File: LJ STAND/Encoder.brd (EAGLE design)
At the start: 24 x 17.4 mm, 4 parts, among them IC1 A1301LH, IC2 A1301LH

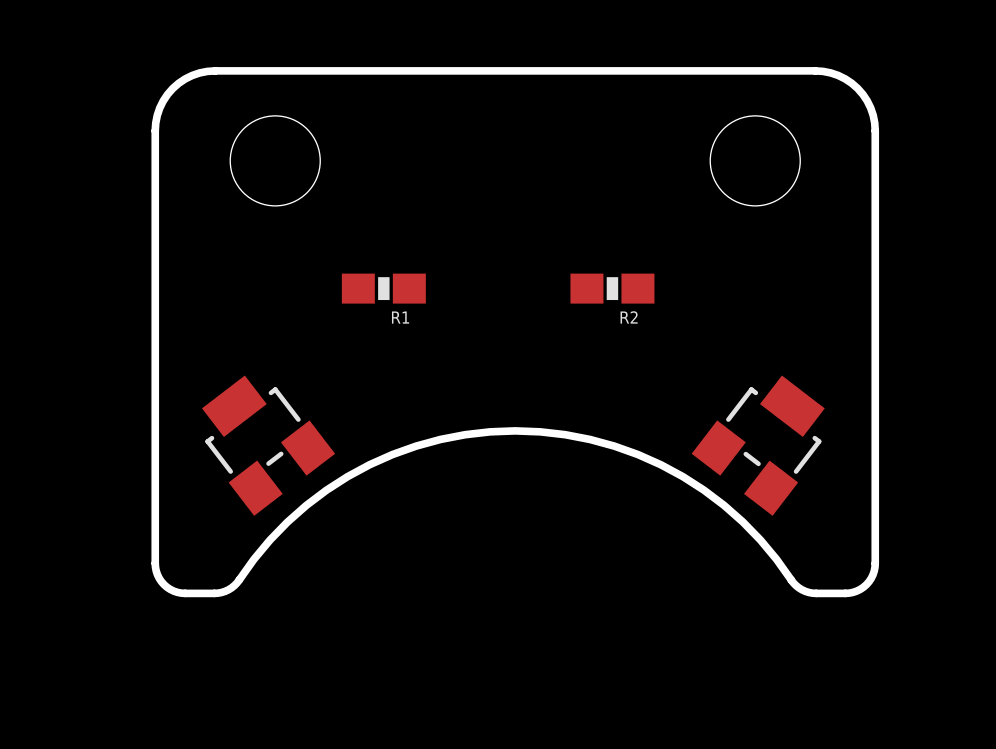
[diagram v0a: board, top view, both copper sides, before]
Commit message: Main & light schematics, preliminary board layout
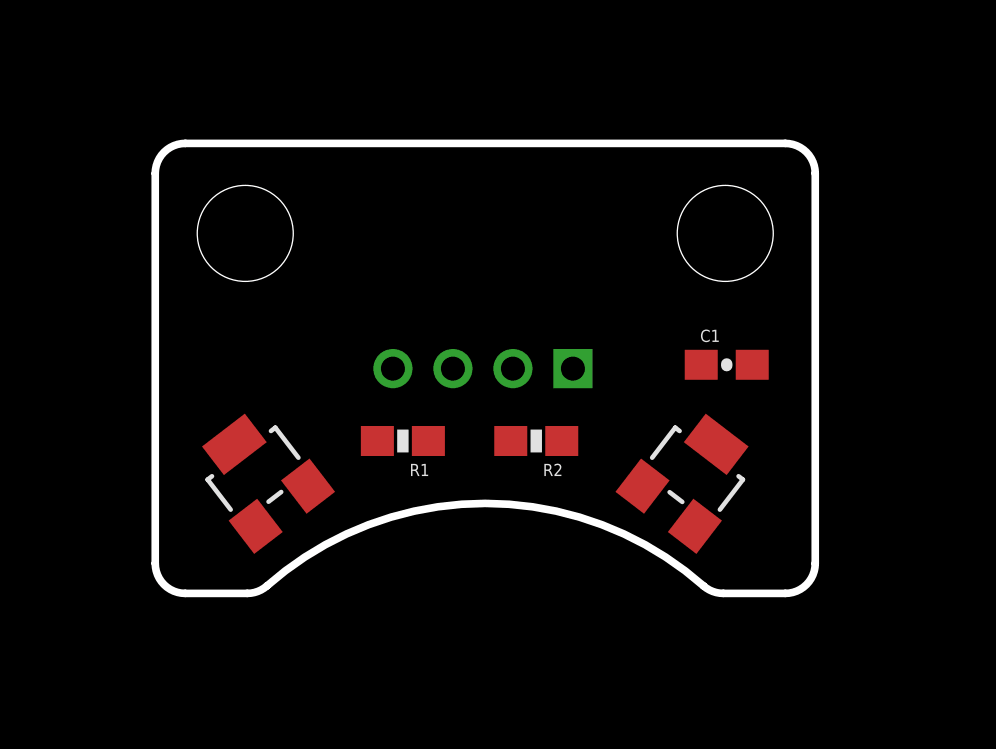
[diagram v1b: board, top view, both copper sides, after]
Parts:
- added C1: 0.1uF, SparkFun-Capacitors:0603-CAP
- added J1: (no value), jst-ph:B4B-PH-K-S
- moved R2 5.68 mm to (12.7, 5.08)
- moved R1 5.12 mm to (8.26, 5.08)
- moved IC2 2.84 mm to (17.9, 3.94)
- moved IC1 1.27 mm to (3.43, 3.94)
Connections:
- net GND: now also C1.2, J1.1
- net OUTA: now also J1.3
- net OUTB: now also J1.2
- net VCC: now also C1.1, J1.4
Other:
- board size 24 x 17.4 mm -> 22 x 15 mm
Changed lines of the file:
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@@
 <?xml version="1.0" encoding="utf-8"?>
 <!DOCTYPE eagle SYSTEM "eagle.dtd">
-<eagle version="8.5.0">
+<eagle version="8.6.3">
 <drawing>
 <settings>
@@
 <setting verticaltext="up"/>
 </settings>
-<grid distance="50" unitdist="mil" unit="mil" style="lines" multiple="1" display="no" altdistance="5" altunitdist="mil" altunit="mil"/>
+<grid distance="25" unitdist="mil" unit="mil" style="lines" multiple="1" display="no" altdistance="5" altunitdist="mil" altunit="mil"/>
 <layers>
 <layer number="1" name="Top" color="4" fill="1" visible="yes" active="yes"/>
@@
 <layer number="112" name="tSilk" color="7" fill="1" visible="yes" active="yes"/>
 <layer number="113" name="IDFDebug" color="4" fill="1" visible="yes" active="yes"/>
+<layer number="114" name="Badge_Outline" color="7" fill="1" visible="yes" active="yes"/>
+<layer number="115" name="ReferenceISLANDS" color="7" fill="1" visible="yes" active="yes"/>
 <layer number="116" name="Patch_BOT" color="9" fill="4" visible="yes" active="yes"/>
+<layer number="118" name="Rect_Pads" color="7" fill="1" visible="yes" active="yes"/>
 <layer number="121" name="_tsilk" color="7" fill="1" visible="yes" active="yes"/>
 <layer number="122" name="_bsilk" color="7" fill="1" visible="yes" active="yes"/>
@@
 </layers>
 <board>
-<fusionsync huburn="a.cGVyc29uYWw6dWUyYWQzYjQx" projecturn="a.cGVyc29uYWw6dWUyYWQzYjQxIzIwMTcxMTAzMTAyMTc0NDI2" f3durn="urn:adsk.wipprod:dm.lineage:2KaG5NQ2SkW999M1W_C92Q" pcbguid="16a91ec9-6d86-41c8-a764-7d3732d7a789" lastpulledtime="2018-02-09T08:51:01Z" lastsyncedchangeguid="f0354a51-48ac-62f3-02b0-e84390e50f97"/>
+<fusionsync huburn="a.cGVyc29uYWw6dWUyYTBjMzI3" projecturn="a.cGVyc29uYWw6dWUyYTBjMzI3IzIwMTgwMjIxMTE4OTc1ODMx" f3durn="urn:adsk.wipprod:dm.lineage:Les9lctRTmKd2iDqQ8lVyw" pcbguid="9d74a9eb-0c4b-4d1f-9566-72efe2af230e" lastpulledtime="2018-02-23T02:58:26Z" lastsyncedchangeguid="d0473fdc-9464-a69d-910f-55a8cdc6a555"/>
 <plain>
-<hole x="4" y="14.41699375" drill="3"/>
-<hole x="20" y="14.41699375" drill="3"/>
-<wire x1="21.1971" y1="0.4514" x2="22.0331" y2="0" width="0.254" layer="20" curve="56.730093"/>
-<wire x1="22.0331" y1="0" x2="23" y2="0" width="0.254" layer="20"/>
-<wire x1="23" y1="0" x2="24" y2="1" width="0.254" layer="20" curve="90"/>
-<wire x1="24" y1="1" x2="24" y2="15.417" width="0.254" layer="20"/>
-<wire x1="24" y1="15.417" x2="22" y2="17.417" width="0.254" layer="20" curve="90"/>
-<wire x1="22" y1="17.417" x2="2" y2="17.417" width="0.254" layer="20"/>
-<wire x1="2" y1="17.417" x2="0" y2="15.417" width="0.254" layer="20" curve="90"/>
-<wire x1="0" y1="15.417" x2="0" y2="1" width="0.254" layer="20"/>
+<hole x="3" y="12" drill="3.2"/>
+<hole x="19" y="12" drill="3.2"/>
+<wire x1="22" y1="1" x2="22" y2="14" width="0.254" layer="20"/>
+<wire x1="22" y1="14" x2="21" y2="15" width="0.254" layer="20" curve="90"/>
+<wire x1="21" y1="15" x2="1" y2="15" width="0.254" layer="20"/>
+<wire x1="1" y1="15" x2="0" y2="14" width="0.254" layer="20" curve="90"/>
+<wire x1="0" y1="14" x2="0" y2="1" width="0.254" layer="20"/>
 <wire x1="0" y1="1" x2="1" y2="0" width="0.254" layer="20" curve="90"/>
-<wire x1="1" y1="0" x2="1.9669" y2="0" width="0.254" layer="20"/>
-<wire x1="1.9669" y1="0" x2="2.8029" y2="0.4514" width="0.254" layer="20" curve="56.730093"/>
-<wire x1="2.8029" y1="0.4514" x2="21.1971" y2="0.4514" width="0.254" layer="20" curve="-113.460187"/>
+<wire x1="1" y1="0" x2="3.063" y2="0" width="0.254" layer="20"/>
+<wire x1="3.063" y1="0" x2="3.724" y2="0.25" width="0.254" layer="20" curve="41.41"/>
+<wire x1="3.724" y1="0.25" x2="18.276" y2="0.25" width="0.254" layer="20" curve="-82.819"/>
+<wire x1="18.276" y1="0.25" x2="18.937" y2="0" width="0.254" layer="20" curve="41.41"/>
+<wire x1="18.937" y1="0" x2="21" y2="0" width="0.254" layer="20"/>
+<wire x1="21" y1="0" x2="22" y2="1" width="0.254" layer="20" curve="90"/>
 </plain>
 <attributes>
@@
 </autorouter>
 <elements>
-<element name="IC1" library="allegro" library_urn="urn:adsk.eagle:library:93" package="SOT23-W" package3d_urn="urn:adsk.eagle:package:3443/1" value="A1301LH" x="3.429" y="5.207" smashed="yes" rot="R37.5">
-<attribute name="MF" value="ALLEGRO MICROSYSTEMS, INC." x="3.429" y="5.207" size="1.778" layer="27" rot="R37.5" display="off"/>
-<attribute name="MPN" value="A1301ELHLT-T" x="3.429" y="5.207" size="1.778" layer="27" rot="R37.5" display="off"/>
-<attribute name="OC_FARNELL" value="1198084" x="3.429" y="5.207" size="1.778" layer="27" rot="R37.5" display="off"/>
-<attribute name="OC_NEWARK" value="31K6634" x="3.429" y="5.207" size="1.778" layer="27" rot="R37.5" display="off"/>
+<element name="IC1" library="allegro" library_urn="urn:adsk.eagle:library:93" package="SOT23-W" package3d_urn="urn:adsk.eagle:package:3443/1" value="A1301LH" x="3.429" y="3.937" smashed="yes" rot="R37.5">
+<attribute name="MF" value="ALLEGRO MICROSYSTEMS, INC." x="3.429" y="3.937" size="1.778" layer="27" rot="R37.5" display="off"/>
+<attribute name="MPN" value="A1301ELHLT-T" x="3.429" y="3.937" size="1.778" layer="27" rot="R37.5" display="off"/>
+<attribute name="OC_FARNELL" value="1198084" x="3.429" y="3.937" size="1.778" layer="27" rot="R37.5" display="off"/>
+<attribute name="OC_NEWARK" value="31K6634" x="3.429" y="3.937" size="1.778" layer="27" rot="R37.5" display="off"/>
 </element>
-<element name="IC2" library="allegro" library_urn="urn:adsk.eagle:library:93" package="SOT23-W" package3d_urn="urn:adsk.eagle:package:3443/1" value="A1301LH" x="20.447" y="5.207" smashed="yes" rot="R322.5">
-<attribute name="MF" value="ALLEGRO MICROSYSTEMS, INC." x="20.447" y="5.207" size="1.778" layer="27" rot="R322.5" display="off"/>
-<attribute name="MPN" value="A1301ELHLT-T" x="20.447" y="5.207" size="1.778" layer="27" rot="R322.5" display="off"/>
-<attribute name="OC_FARNELL" value="1198084" x="20.447" y="5.207" size="1.778" layer="27" rot="R322.5" display="off"/>
-<attribute name="OC_NEWARK" value="31K6634" x="20.447" y="5.207" size="1.778" layer="27" rot="R322.5" display="off"/>
+<element name="IC2" library="allegro" library_urn="urn:adsk.eagle:library:93" package="SOT23-W" package3d_urn="urn:adsk.eagle:package:3443/1" value="A1301LH" x="17.907" y="3.937" smashed="yes" rot="R322.5">
+<attribute name="MF" value="ALLEGRO MICROSYSTEMS, INC." x="17.907" y="3.937" size="1.778" layer="27" rot="R322.5" display="off"/>
+<attribute name="MPN" value="A1301ELHLT-T" x="17.907" y="3.937" size="1.778" layer="27" rot="R322.5" display="off"/>
+<attribute name="OC_FARNELL" value="1198084" x="17.907" y="3.937" size="1.778" layer="27" rot="R322.5" display="off"/>
+<attribute name="OC_NEWARK" value="31K6634" x="17.907" y="3.937" size="1.778" layer="27" rot="R322.5" display="off"/>
 </element>
-<element name="R1" library="SparkFun-Resistors" package="0603-RES" value="10K" x="7.62" y="10.16" rot="R180"/>
-<element name="R2" library="SparkFun-Resistors" package="0603-RES" value="10K" x="15.24" y="10.16" rot="R180"/>
+<element name="R1" library="SparkFun-Resistors" package="0603-RES" value="10K" x="8.255" y="5.08" rot="R180"/>
+<element name="R2" library="SparkFun-Resistors" package="0603-RES" value="10K" x="12.7" y="5.08" rot="R180"/>
+<element name="C1" library="SparkFun-Capacitors" package="0603-CAP" value="0.1uF" x="19.05" y="7.62"/>
+<element name="J1" library="jst-ph" library_urn="urn:adsk.eagle:library:1951258" package="B4B-PH-K-S" package3d_urn="urn:adsk.eagle:package:1951337/2" value="" x="10.922" y="7.493" smashed="yes" rot="MR0"/>
 </elements>
 <signals>
@@
 <contactref element="IC1" pad="2"/>
 <contactref element="R1" pad="1"/>
-<wire x1="8.47" y1="10.16" x2="5.093078125" y2="4.845278125" width="0" layer="19" extent="1-1"/>
+<contactref element="J1" pad="3"/>
+<wire x1="5.093078125" y1="3.575278125" x2="9.105" y2="5.08" width="0" layer="19" extent="1-1"/>
+<wire x1="9.922" y1="7.493" x2="5.093078125" y2="3.575278125" width="0" layer="19" extent="1-1"/>
 </signal>
 <signal name="OUTB">
 <contactref element="IC2" pad="2"/>
 <contactref element="R2" pad="1"/>
-<wire x1="16.09" y1="10.16" x2="20.528296875" y2="3.506" width="0" layer="19" extent="1-1"/>
+<contactref element="J1" pad="2"/>
+<wire x1="17.988296875" y1="2.236" x2="13.55" y2="5.08" width="0" layer="19" extent="1-1"/>
+<wire x1="11.922" y1="7.493" x2="17.988296875" y2="2.236" width="0" layer="19" extent="1-1"/>
 </signal>
 <signal name="VCC">
@@
 <contactref element="IC2" pad="1"/>
 <contactref element="R2" pad="2"/>
-<wire x1="6.77" y1="10.16" x2="3.3477" y2="3.506" width="0" layer="19" extent="1-1"/>
-<wire x1="18.78291875" y1="4.845278125" x2="6.77" y2="10.16" width="0" layer="19" extent="1-1"/>
-<wire x1="14.39" y1="10.16" x2="18.78291875" y2="4.845278125" width="0" layer="19" extent="1-1"/>
+<contactref element="C1" pad="1"/>
+<contactref element="J1" pad="4"/>
+<wire x1="11.85" y1="5.08" x2="16.24291875" y2="3.575278125" width="0" layer="19" extent="1-1"/>
+<wire x1="18.2" y1="7.62" x2="11.85" y2="5.08" width="0" layer="19" extent="1-1"/>
+<wire x1="7.405" y1="5.08" x2="18.2" y2="7.62" width="0" layer="19" extent="1-1"/>
+<wire x1="3.3477" y1="2.236" x2="7.405" y2="5.08" width="0" layer="19" extent="1-1"/>
+<wire x1="7.922" y1="7.493" x2="16.24291875" y2="3.575278125" width="0" layer="19" extent="1-1"/>
 </signal>
 <signal name="GND">
 <contactref element="IC1" pad="3"/>
 <contactref element="IC2" pad="3"/>
-<wire x1="21.2383875" y1="6.23835625" x2="2.637609375" y2="6.23835625" width="0" layer="19" extent="1-1"/>
+<contactref element="C1" pad="2"/>
+<contactref element="J1" pad="1"/>
+<wire x1="19.9" y1="7.62" x2="18.6983875" y2="4.96835625" width="0" layer="19" extent="1-1"/>
+<wire x1="2.637609375" y1="4.96835625" x2="19.9" y2="7.62" width="0" layer="19" extent="1-1"/>
+<wire x1="13.922" y1="7.493" x2="2.637609375" y2="4.96835625" width="0" layer="19" extent="1-1"/>
 </signal>
 </signals>

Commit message: Finished routing light & encoder pcbs
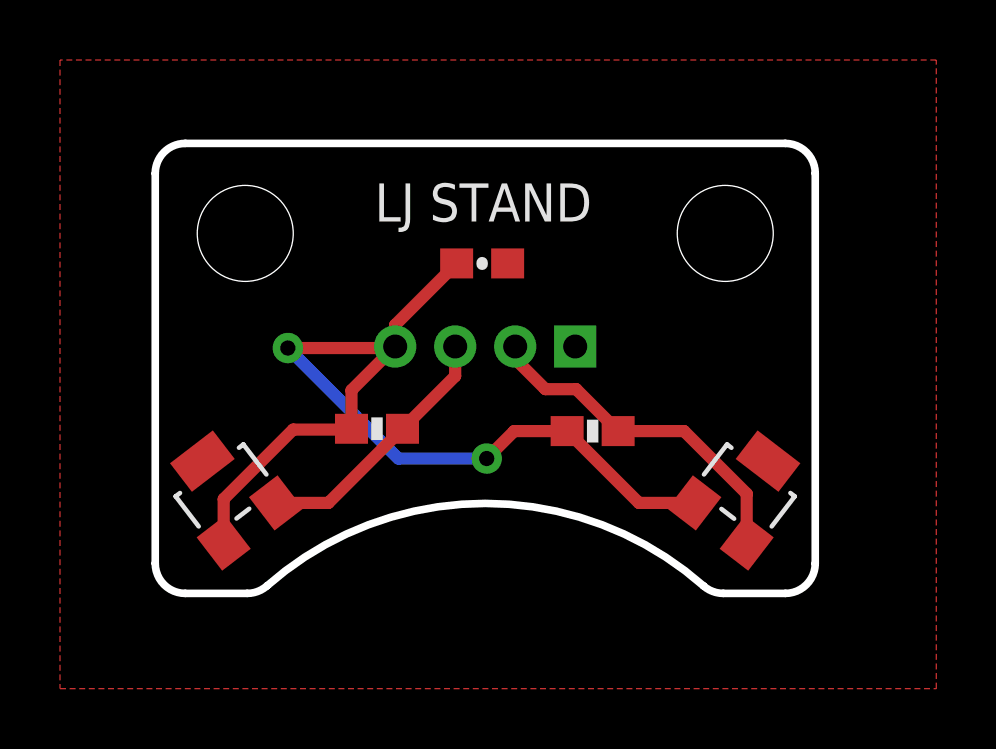
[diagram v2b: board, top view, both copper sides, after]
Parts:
- moved C1 8.83 mm to (10.9, 11.0)
- moved R2 1.91 mm to (14.6, 5.41)
- moved IC2 1.82 mm to (19.6, 3.38)
- moved IC1 1.20 mm to (2.36, 3.38)
- moved R1 0.95 mm to (7.39, 5.49)
- moved J1 0.74 mm to (11.0, 8.23)
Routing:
- net VCC: track 0.00 -> 33.7 mm, vias 0 -> 2
- net OUTB: track 0.00 -> 11.6 mm
- net OUTA: track 0.00 -> 8.71 mm
- added copper zone on layer 1, net GND
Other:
- board text added: "GND"
- board text added: "LJ STAND"
- board text added: "OUTA"
- board text added: "OUTB"
- board text added: "VCC"
